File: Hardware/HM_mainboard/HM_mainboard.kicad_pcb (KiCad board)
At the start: 2 copper layers, 80 x 55 mm, 58 parts, among them J1 JST PH2P ST90, J2 USB4105-GF-A, J3 Conn_01x04, J4 54-00174, J5 54-00174, J6 54-00174, J7 54-00174, Q1 PMOS AS3401, U1 MCP73831-2, U2 TC1262-33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

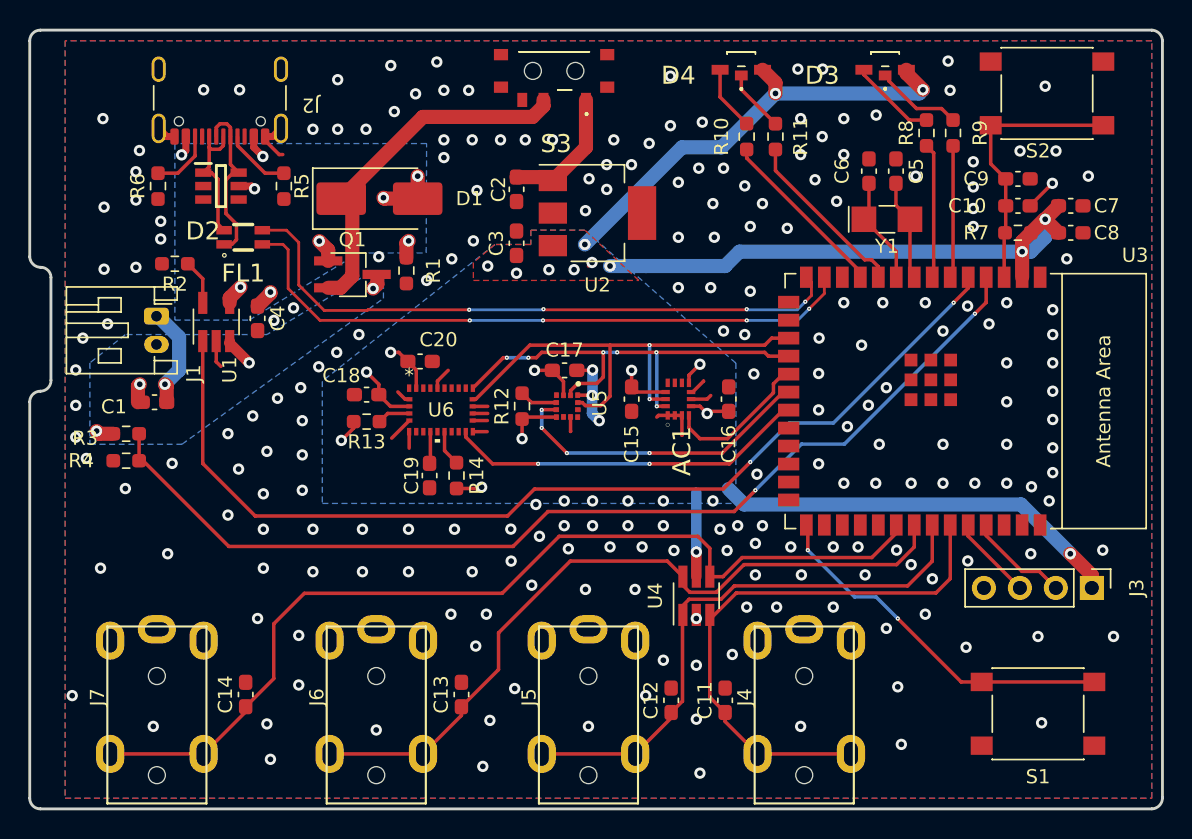
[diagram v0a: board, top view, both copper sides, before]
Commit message: Added testpoints to pcb
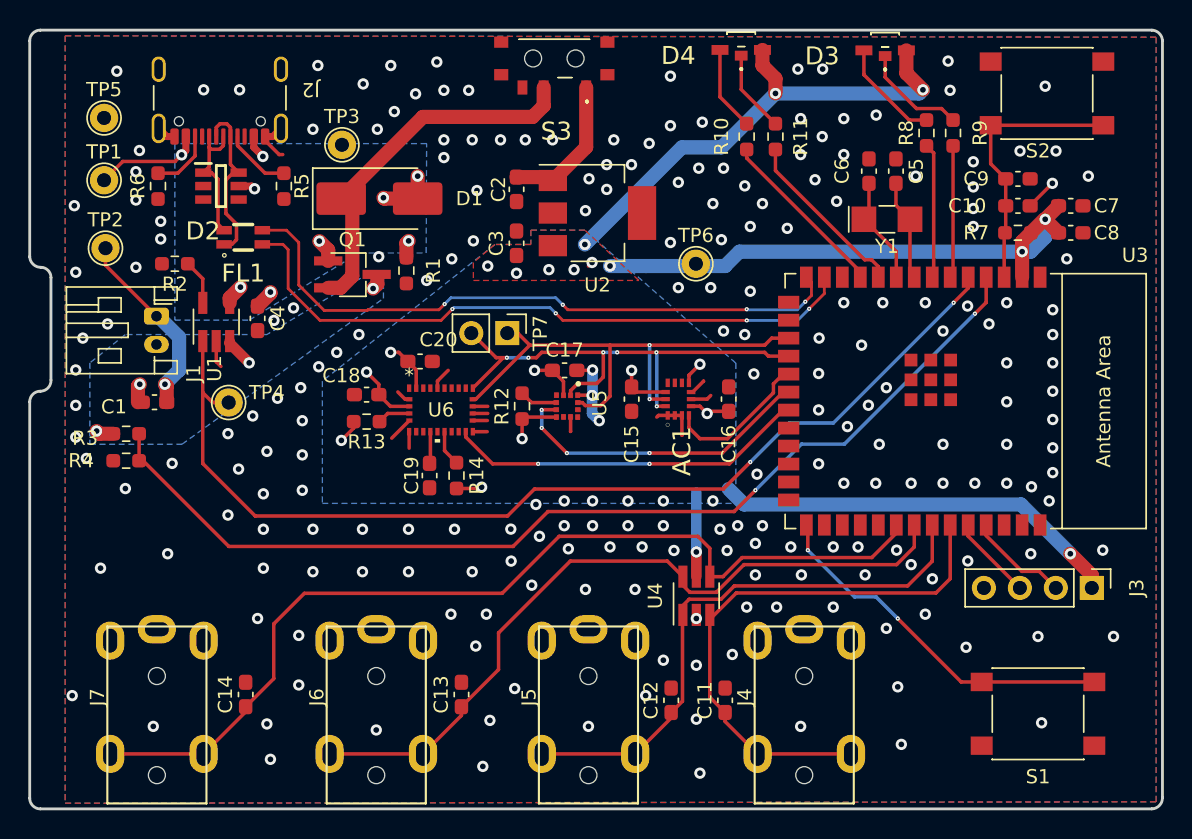
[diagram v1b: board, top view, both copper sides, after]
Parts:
- added TP1: TestPoint_Probe, TestPoint:TestPoint_THTPad_D2.0mm_Drill1.0mm, F.Cu at (122.0, 83.6)
- added TP2: TestPoint_Probe, TestPoint:TestPoint_THTPad_D2.0mm_Drill1.0mm, F.Cu at (122.1, 88.4)
- added TP3: TestPoint_Probe, TestPoint:TestPoint_THTPad_D2.0mm_Drill1.0mm, F.Cu at (138.8, 81.1)
- added TP4: TestPoint_Probe, TestPoint:TestPoint_THTPad_D2.0mm_Drill1.0mm, F.Cu at (130.8, 99.3)
- added TP5: TestPoint_Probe, TestPoint:TestPoint_THTPad_D2.0mm_Drill1.0mm, F.Cu at (122.0, 79.2)
- added TP6: TestPoint_Probe, TestPoint:TestPoint_THTPad_D2.0mm_Drill1.0mm, F.Cu at (163.8, 89.5)
- added TP7: TestPoint_2Pole, Connector_PinHeader_2.54mm:PinHeader_1x02_P2.54mm_Vertical, F.Cu at (150.5, 94.4)
- moved D4 1.40 mm to (167.0, 74.8)
- moved D3 1.37 mm to (177.2, 74.8)
- moved S3 0.88 mm to (153.8, 75.0)
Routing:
- net V_BATT: track 11.4 -> 17.7 mm
- net V_USB: track 14.5 -> 20.8 mm
- net /I2C_SDA: track 32.7 -> 35.6 mm
- net 3.3V: track 135.4 -> 138.2 mm
- net /BATT_CHARGING_STATUS: track 71.7 -> 73.8 mm
- net /I2C_SCL: track 35.3 -> 37.2 mm
- net Net-(D4-K1): track 4.40 -> 5.81 mm
- net Net-(D4-K2): track 4.58 -> 5.99 mm
- net Net-(D3-K1): track 6.18 -> 7.55 mm
- net Net-(D3-K2): track 6.10 -> 7.47 mm
- net /Battery_and_Power_Managment/V_PWR_SWITCH: track 25.5 -> 26.4 mm
- net /Battery_and_Power_Managment/V_IN: track 9.32 -> 10.2 mm
- net /Microcontroller - ESP32-S3-WROOM/USB_C_D-: track 45.5 -> 46.2 mm
- net /Microcontroller - ESP32-S3-WROOM/USB_C_D+: track 44.8 -> 45.5 mm

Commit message: Added gerber files and schematic printed to pdf
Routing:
- net /Battery_and_Power_Managment/V_PWR_SWITCH: track 26.4 -> 29.4 mm
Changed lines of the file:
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@@
       (drillshape 0)
       (scaleselection 1)
-      (outputdirectory "")
+      (outputdirectory "Gerber/V1.0.1/")
     )
   )
@@
   (segment (start 183.03 108.745) (end 186.68 112.395) (width 0.25) (layer "F.Cu") (net 34))
   (segment (start 183.03 107.95) (end 183.03 108.745) (width 0.25) (layer "F.Cu") (net 34))
+  (segment (start 138.8 81.1) (end 140.174 82.474) (width 0.25) (layer "F.Cu") (net 35))
   (segment (start 139.53 85.682) (end 138.748 84.9) (width 1) (layer "F.Cu") (net 35))
   (segment (start 139.53 90.37) (end 139.53 85.682) (width 1) (layer "F.Cu") (net 35))
@@
   (segment (start 137.83 91.2) (end 138.7 91.2) (width 1) (layer "F.Cu") (net 35))
   (segment (start 144.518 79.13) (end 152.264 79.13) (width 1) (layer "F.Cu") (net 35))
-  (segment (start 138.748 84.9) (end 144.518 79.13) (width 1) (layer "F.Cu") (net 35))
   (segment (start 153.05 78.344) (end 153.05 77.05) (width 1) (layer "F.Cu") (net 35))
+  (segment (start 141.174 82.474) (end 144.518 79.13) (width 1) (layer "F.Cu") (net 35))
+  (segment (start 138.748 84.9) (end 141.174 82.474) (width 1) (layer "F.Cu") (net 35))
   (segment (start 138.7 91.2) (end 139.53 90.37) (width 1) (layer "F.Cu") (net 35))
+  (segment (start 140.174 82.474) (end 141.174 82.474) (width 0.25) (layer "F.Cu") (net 35))
   (segment (start 168 105.5) (end 166.5 107) (width 0.25) (layer "F.Cu") (net 36))
   (segment (start 153.35 107) (end 150.885305 109.464695) (width 0.25) (layer "F.Cu") (net 36))

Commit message: Improved pcb layout design
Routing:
- net GND: vias 228 -> 256
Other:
- board size 80 x 55 mm -> 79.5 x 55 mm

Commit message: Moved a wire
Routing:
- net V_BATT: track 17.7 -> 13.8 mm
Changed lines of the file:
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@@
   (via (at 143.51 87.884) (size 0.8) (drill 0.4) (layers "F.Cu" "B.Cu") (net 10))
   (via (at 127.477496 81.809906) (size 0.8) (drill 0.4) (layers "F.Cu" "B.Cu") (net 10))
+  (segment (start 126.4 98.1) (end 126.426 98.126) (width 0.25) (layer "F.Cu") (net 11))
+  (segment (start 126.426 98.126) (end 126.426 99.281) (width 1) (layer "F.Cu") (net 11))
   (segment (start 121.666 101.506) (end 121.473 101.313) (width 1) (layer "F.Cu") (net 11))
   (segment (start 141.3 90.95) (end 141 91.25) (width 1) (layer "F.Cu") (net 11))
@@
   (segment (start 122.1 89.6) (end 125.701 93.201) (width 0.25) (layer "F.Cu") (net 11))
   (segment (start 132.25 96.5) (end 130.871 95.121) (width 0.75) (layer "F.Cu") (net 11))
-  (segment (start 126.426 98.138) (end 126.299 98.011) (width 1) (layer "F.Cu") (net 11))
   (segment (start 122.649 101.506) (end 121.666 101.506) (width 1) (layer "F.Cu") (net 11))
-  (segment (start 126.426 99.281) (end 126.426 98.138) (width 1) (layer "F.Cu") (net 11))
   (segment (start 122.1 88.4) (end 122.1 89.6) (width 0.25) (layer "F.Cu") (net 11))
   (segment (start 141.3 90.6) (end 141.3 90.95) (width 1) (layer "F.Cu") (net 11))
-  (via (at 126.299 98.011) (size 0.8) (drill 0.4) (layers "F.Cu" "B.Cu") (net 11))
+  (via (at 126.4 98.1) (size 0.8) (drill 0.4) (layers "F.Cu" "B.Cu") (net 11))
   (via (at 132.25 96.5) (size 0.8) (drill 0.4) (layers "F.Cu" "B.Cu") (net 11))
   (via (at 121.473 101.313) (size 0.8) (drill 0.4) (layers "F.Cu" "B.Cu") (net 11))
@@
   (segment (start 127.3 94.686522) (end 125.814478 93.201) (width 1) (layer "B.Cu") (net 11))
   (segment (start 125.814478 93.201) (end 125.701 93.201) (width 1) (layer "B.Cu") (net 11))
-  (segment (start 126.299 98.011) (end 127.3 97.01) (width 1) (layer "B.Cu") (net 11))
-  (segment (start 127.3 97.01) (end 127.3 94.686522) (width 1) (layer "B.Cu") (net 11))
   (segment (start 178.917 90.147) (end 179.22 90.45) (width 0.25) (layer "F.Cu") (net 12))
   (segment (start 177.927 85.37) (end 178.917 86.36) (width 0.25) (layer "F.Cu") (net 12))

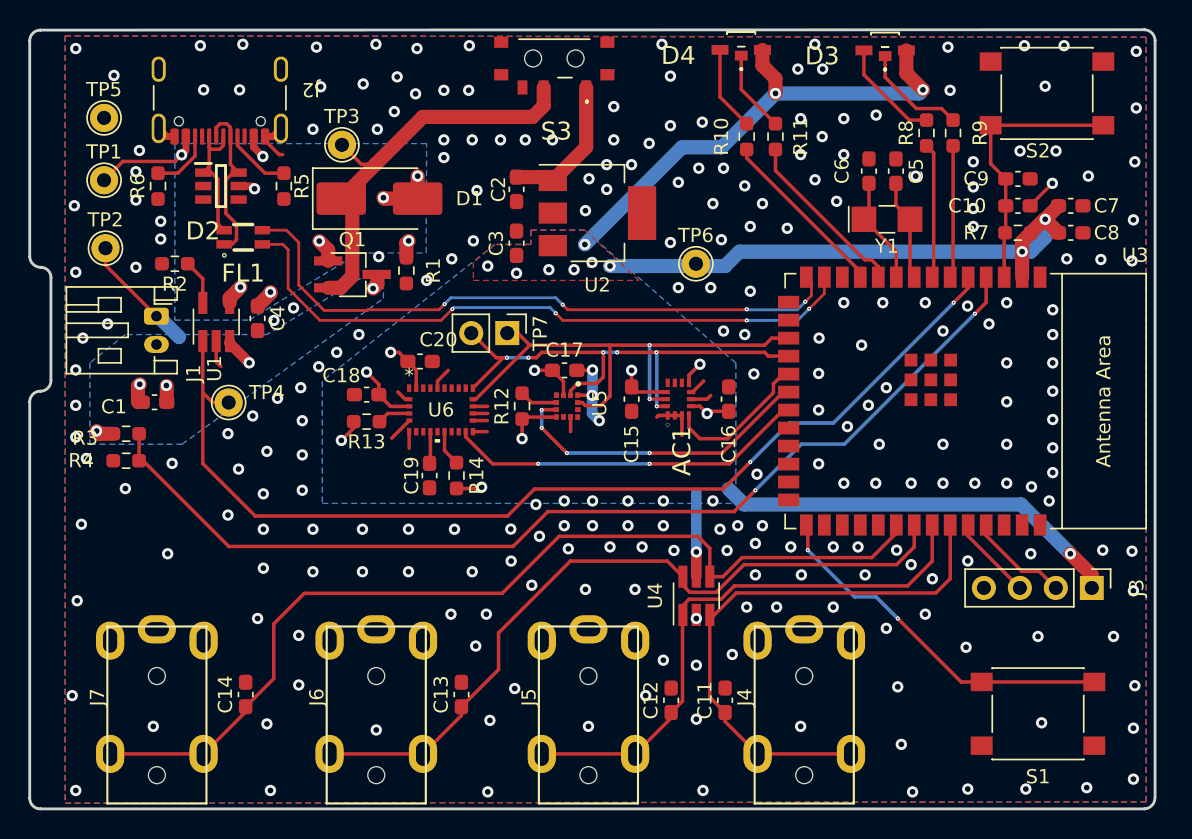
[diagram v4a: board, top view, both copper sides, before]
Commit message: Added connector for sip&puff sensor
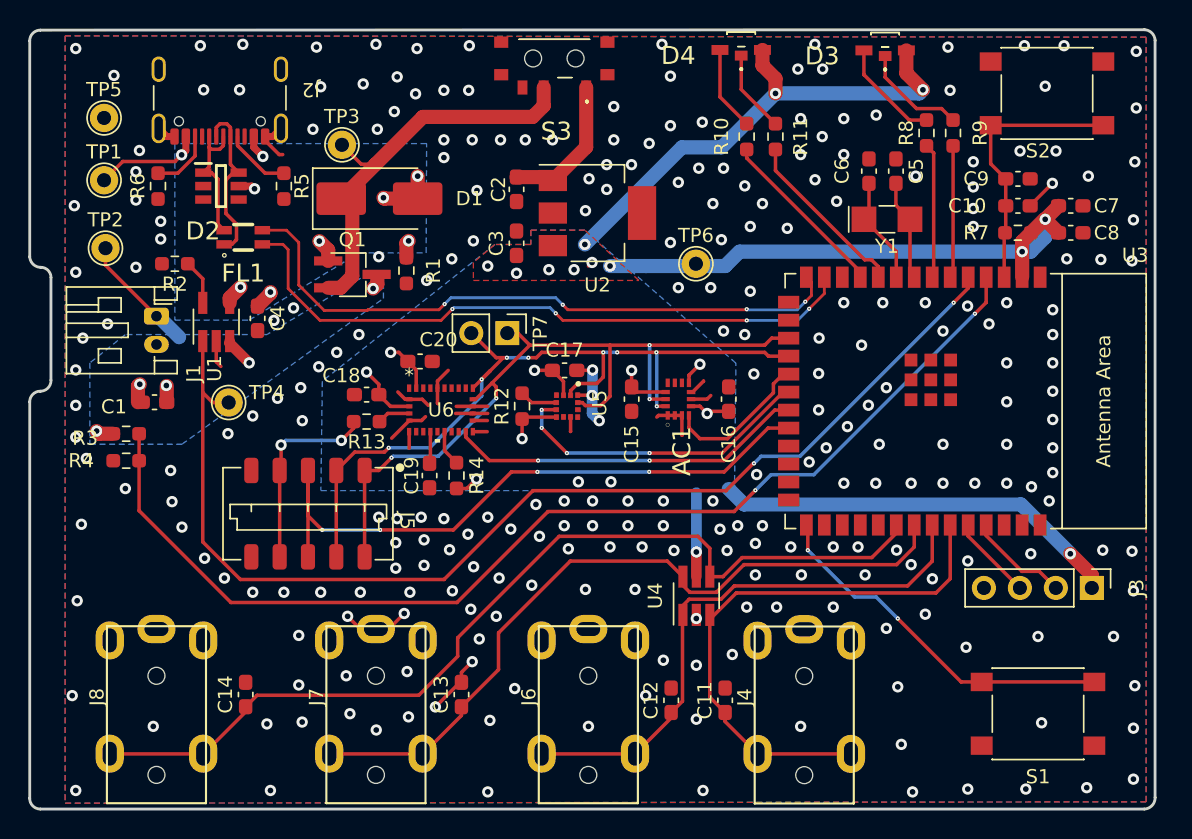
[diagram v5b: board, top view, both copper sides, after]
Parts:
- added J8: 54-00174, HeadMouse:54-00174, F.Cu at (125.7, 127.6)
- J5: value 54-00174 -> 009159005551906; footprint HeadMouse:54-00174 -> HeadMouse:009159005551906
- moved J5 28.5 mm to (136.4, 107.2), turned to 0 degrees
- moved J7 15.5 mm to (141.2, 127.6)
- moved J6 15.0 mm to (156.2, 127.6)
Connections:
- J5 pad 1: GND -> /I2C_SCL
- J5 pad 2: GND -> /I2C_SDA
- J5 pad 3: GND -> /MPRLS_INT
- J5 pad 4: /BTN_2 -> 3.3V
- J5 pad 5: /BTN_2 -> GND
- J6 pad 4: /BTN_3 -> /BTN_2
- J6 pad 5: /BTN_3 -> /BTN_2
- J7 pad 4: /BTN_4 -> /BTN_3
- J7 pad 5: /BTN_4 -> /BTN_3
- U3 pad 22: /Microcontroller - ESP32-S3-WROOM/GPIO_14 -> /MPRLS_INT
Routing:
- net /MPRLS_INT: track 0.00 -> 46.6 mm, vias 0 -> 4
- net /I2C_SDA: track 35.6 -> 56.2 mm, vias 6 -> 8
- net /I2C_SCL: track 37.2 -> 55.9 mm, vias 2 -> 4
- net GND: track 32.8 -> 48.2 mm, vias 256 -> 272
- net 3.3V: track 138.2 -> 150.4 mm, vias 22 -> 23
- net /BATT_CHARGING_STATUS: track 73.8 -> 80.8 mm
- net /V_BATT_MEASURE: track 73.2 -> 78.5 mm
- net /BTN_4: track 68.6 -> 67.1 mm
